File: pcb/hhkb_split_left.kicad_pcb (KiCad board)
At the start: 4 copper layers, 140.4 x 97.4 mm, 68 parts, among them SW1 Esc, SW10 E, SW11 R, SW12 T, SW13 Ctrl, SW14 A, SW15 S, SW16 D, SW17 F, SW18 G, SW19 Shift, SW2 1, SW20 Z, SW21 X, SW22 C, SW23 V, SW24 B, SW25 Alt, SW26 Meta, SW27 L-Space, SW3 2, SW4 3, SW5 4, SW6 5, SW7 Tab, SW8 Q, SW9 W, U1 74HC595

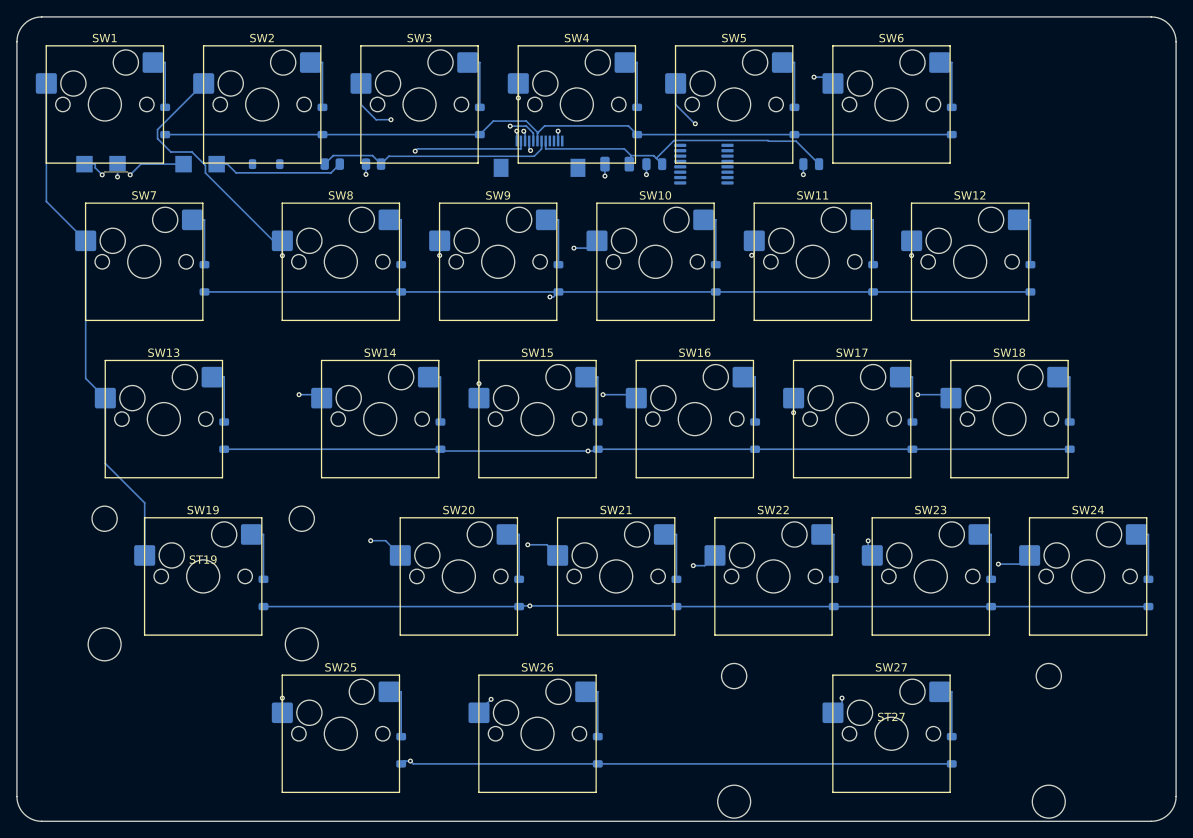
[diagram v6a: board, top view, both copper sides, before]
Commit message: マトリクスのダイオードを SD103AW にした（打ち止めが保証値で決まる）
1N4148W は **1mA 未満の Vf 最大値を規定していない**。行に届くのは
（レール − Vf）で nRF52840 の VIH は 0.7×レール、つまり レール ≧ Vf/0.3。
1mA の最大 0.715V で詰めるとレール 2.55V（1.48V/本）が必要になり、
**打ち止めが 1.12〜1.48V/本 の間で不定だった。電池が減るとキーが
反応しなくなる。**

SD103AW（C130875）は **VF ≦ 0.37V @ 20mA を保証**している。実使用は
100µA でそれよりはるかに小さい。必要なレールは 1.40V で、マイコンの
1.80V の内側。**打ち止めはマイコン律速の 1.10V/本 に戻った。実測不要。**

  逆漏れ 5µA @ 30V（実使用 2V ではさらに小さい）。プルダウン 13kΩ に対し
  誤検出には 20 個以上の同時押しが要る
  フットプリントは同じ SOD-123。**基板は変わらない**（Value は B.Fab のみ）
  単価 $0.0116 で 1N4148W とほぼ同じ。Basic → Extended で +$3

3 基板とも DRC 0 / 未配線 0。検査 292 件。部品 8 種すべて在庫を再確認した。
C4 からダイオードの実測手順を削り、provisional-values から
MATRIX_DIODE_VF を外した（保証値になったため）。

Co-Authored-By: Claude Opus 5 (1M context) <noreply@anthropic.com>
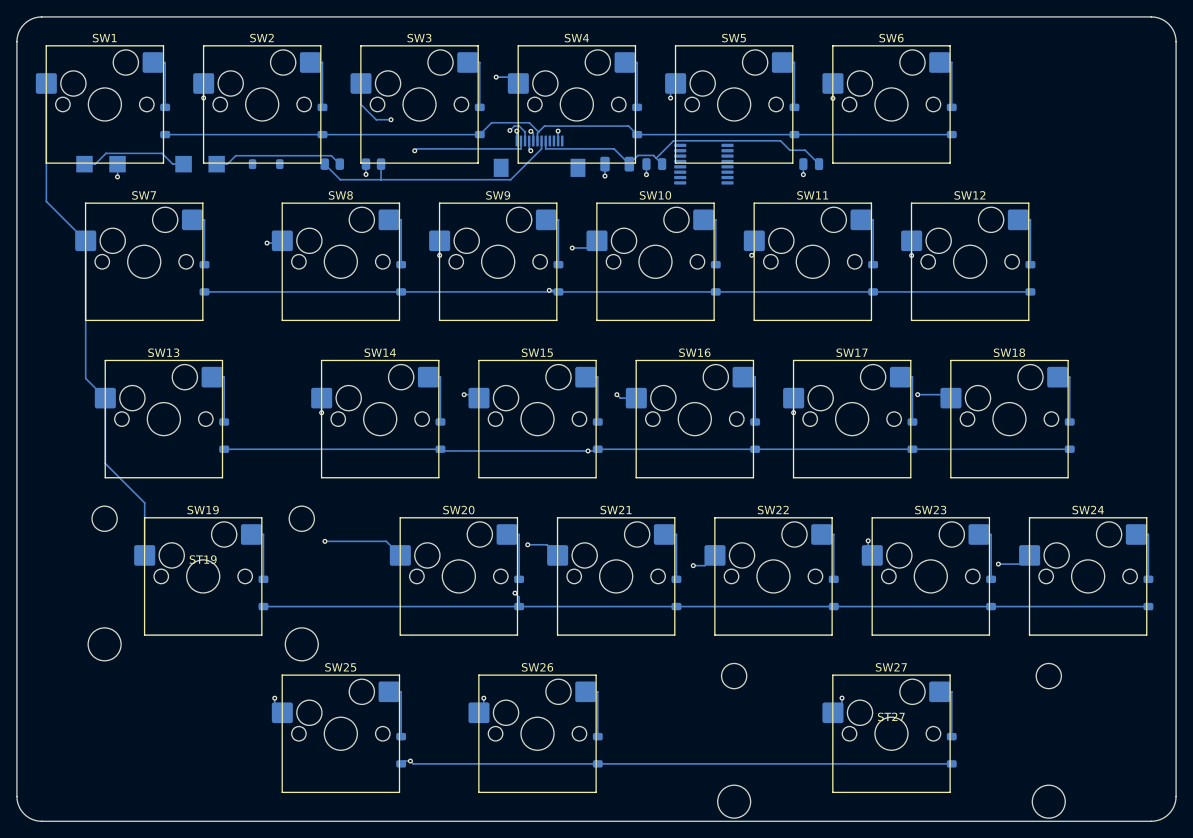
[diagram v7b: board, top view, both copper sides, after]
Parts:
- D1, D10, D11, D12, D13, D14, D15, D16, D17, D18, D19, D2, D20, D21, D22, D23, D24, D25, D26, D27, D3, D4, D5, D6, D7, D8, D9: value 1N4148W -> SD103AW
- U1: value 74HC595 -> 74LVC595
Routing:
- net ROW1: track 128.3 -> 123.8 mm
- net COL5: track 112.1 -> 107.8 mm
- net COL1: track 103.0 -> 98.8 mm, vias 4 -> 5
- net ROW3: track 170.9 -> 174.5 mm
- net COL3: track 111.2 -> 114.7 mm
- net VBATT_SENSE: track 28.8 -> 31.4 mm
- net ROW4: track 155.8 -> 157.5 mm
- net VBATT_RAW: track 13.6 -> 13.1 mm, vias 2 -> 0

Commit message: マトリクスのダイオードを 1N4148W へ戻した（SD103AW への変更は誤り）
効く parameter は 2 つあり、片方だけ見て替えたため取り替えっこになっていた。

  (a) 走査電流での Vf … 行に届くのは（レール − Vf）。レール ≧ Vf/0.3
  (b) 逆漏れ … ダイオード本来の役目（ゴースト防止）

  型番      (a) Vf の保証         (b) 逆漏れの保証    単価/305個
  1N4148W   なし(1mA で 0.715V)   25nA @ 20V          $3.57 Basic ← 採用
  SD103AW   0.37V @ 20mA          なし(30V で 5µA)    $3.54 +$3
  BAT46W    250mV @ 0.1mA         0.5µA @ 1.5V        $28.1 +$3

SD103AW は逆漏れの保証が動作点に無い。30V の 5µA を当てると、
プルダウン 13kΩ に対して **2 個同時押しでもゴーストの margin を割る**
（引き下げ 130mV に対し余裕 120mV）。**誤った文字が出る側の失敗**なので、
打ち止めが不定であることより害が大きい。

1N4148W は逆漏れが桁違いに小さく本来の役目は保証される。不定なのは
打ち止めだけで、これは「電池が早く終わる」であって誤動作ではない。

BAT46W は両方を動作点で保証する唯一の候補（VF ≦ 250mV @ 0.1mA、
IR ≦ 0.5µA @ 1.5V）。**+$24.5（¥3,700）。**実測が難しければここへ戻る。

C4 の測定手順を戻した。**1N4007 では測れない**ことを明記した（接合が
大きく Vf が低く出る）。1N4148 が無ければ測定は飛ばしてよい。

3 基板とも DRC 0 / 未配線 0。検査 292 件。

Co-Authored-By: Claude Opus 5 (1M context) <noreply@anthropic.com>
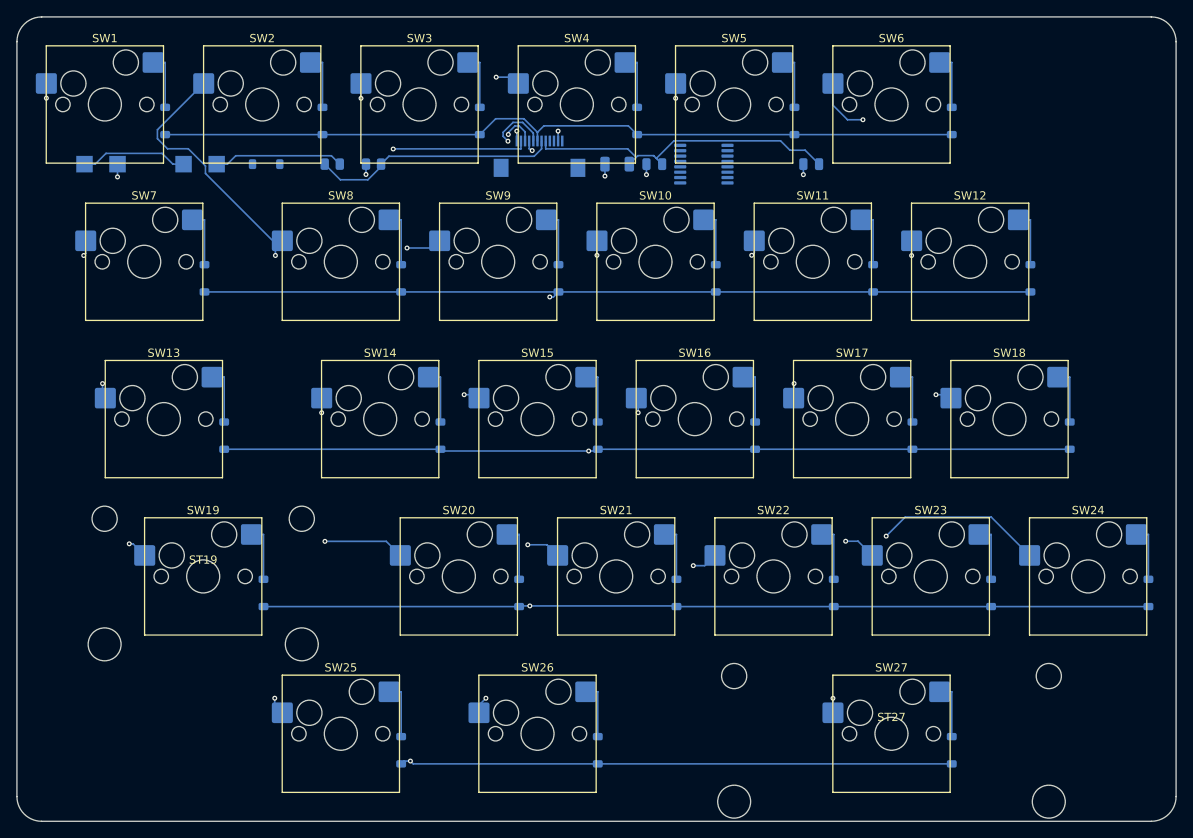
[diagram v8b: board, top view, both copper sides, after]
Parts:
- D1, D10, D11, D12, D13, D14, D15, D16, D17, D18, D19, D2, D20, D21, D22, D23, D24, D25, D26, D27, D3, D4, D5, D6, D7, D8, D9: value SD103AW -> 1N4148W
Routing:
- net ROW1: track 123.8 -> 129.5 mm
- net COL1: track 98.8 -> 104.3 mm, vias 5 -> 4
- net COL0: track 62.1 -> 66.1 mm, vias 0 -> 4
- net COL5: track 107.8 -> 111.6 mm
- net COL3: track 114.7 -> 112.1 mm
- net ROW4: track 157.5 -> 159.7 mm
- net VBATT_SENSE: track 31.4 -> 29.7 mm
- net COL2: track 73.2 -> 74.7 mm
- net ROW2: track 144.8 -> 143.5 mm
- net ROW3: track 174.5 -> 174.0 mm
